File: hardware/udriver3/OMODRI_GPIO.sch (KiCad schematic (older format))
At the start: 5 parts, among them J14 Conn_01x40, U1 TMS320F28388D, U15 TPD2E001, U16 TPD3E001, U6 TPD3E001

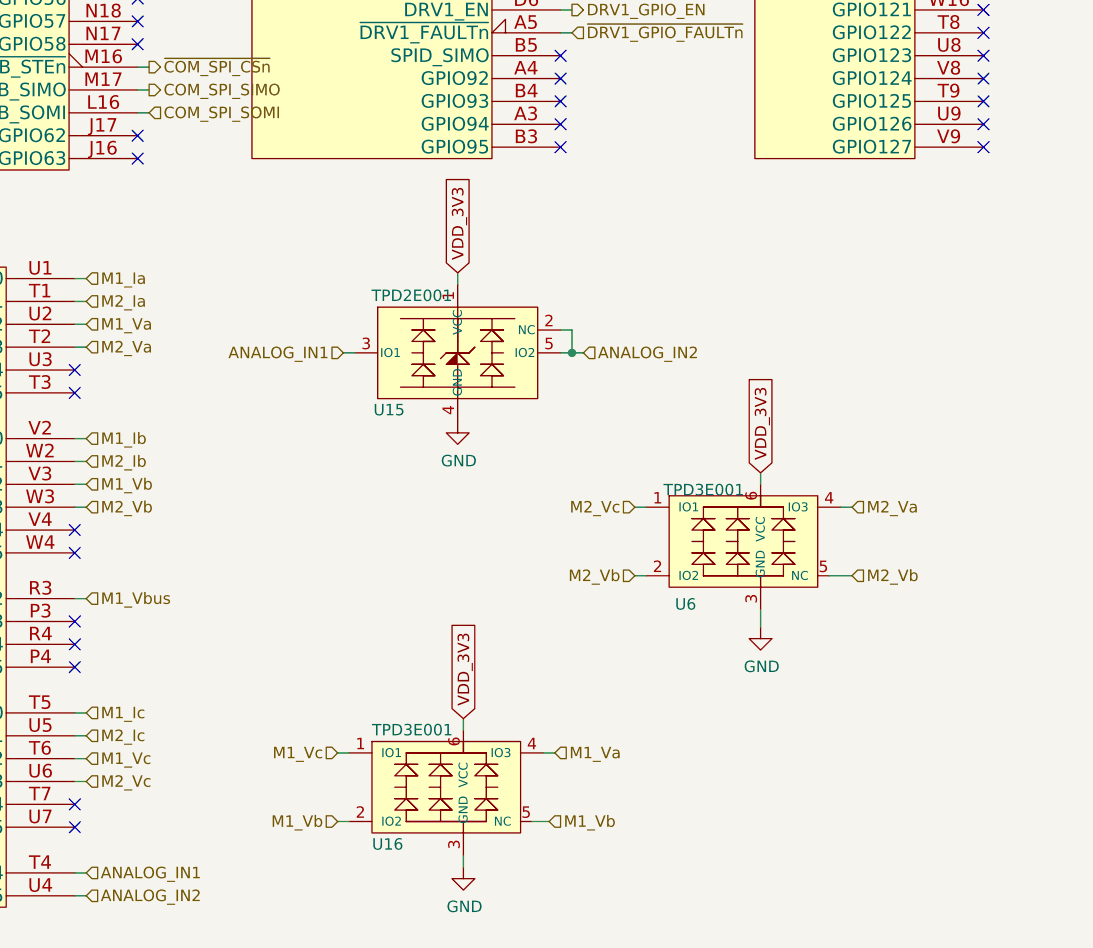
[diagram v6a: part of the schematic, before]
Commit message: Routing update. All analog and DRV signals are wired. TMS mcu decoupling capacitors are in place.
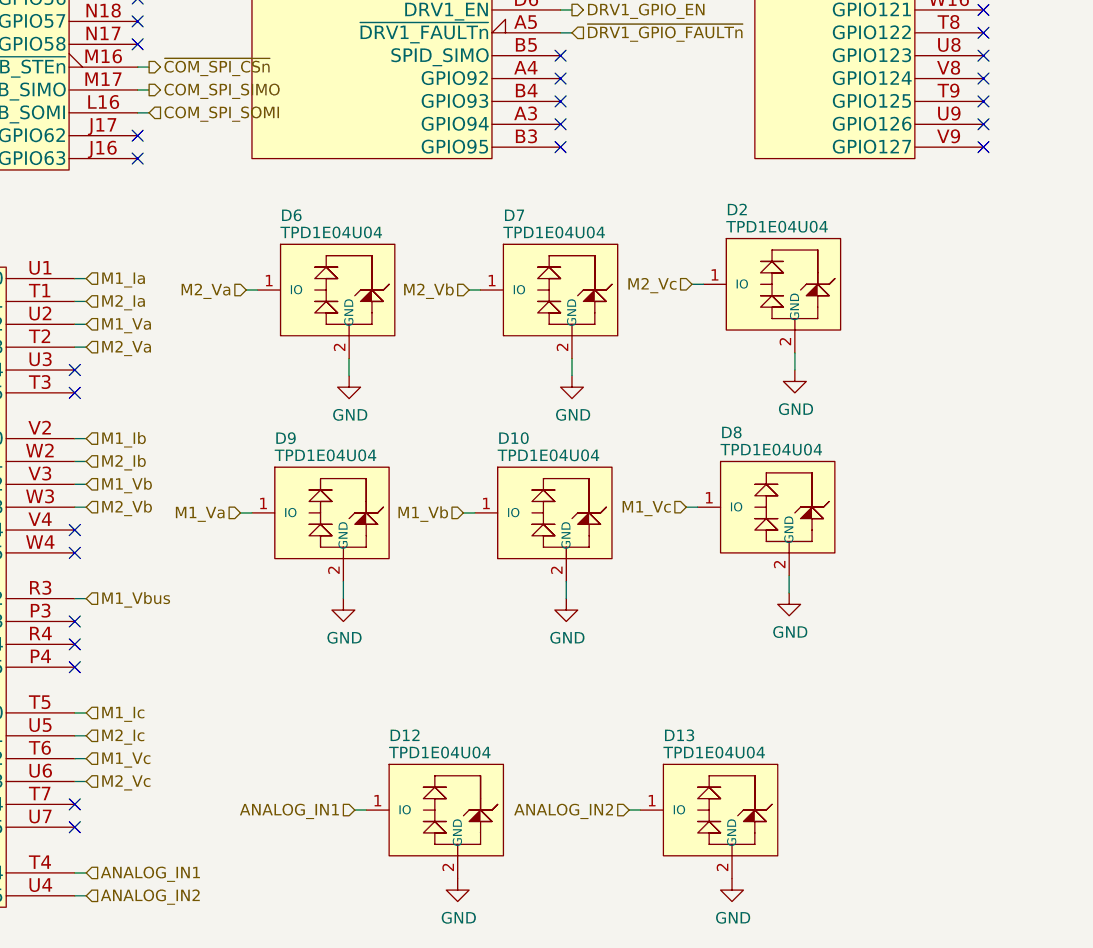
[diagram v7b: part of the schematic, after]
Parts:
- removed U15: TPD2E001, Package_SO:Texas_R-PDSO-N5, symbol omodri_lib:TPD2E001
- removed U16, U6: TPD3E001, udriver3:USON_6, symbol omodri_lib:TPD3E001
- added D10, D12, D13, D2, D6, D7, D8, D9: TPD1E04U04, Diode_SMD:D_0201_0603Metric, symbol omodri_lib:TPD1E04U04
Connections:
- net labels removed: VDD_3V3
- wire segments 177 -> 173

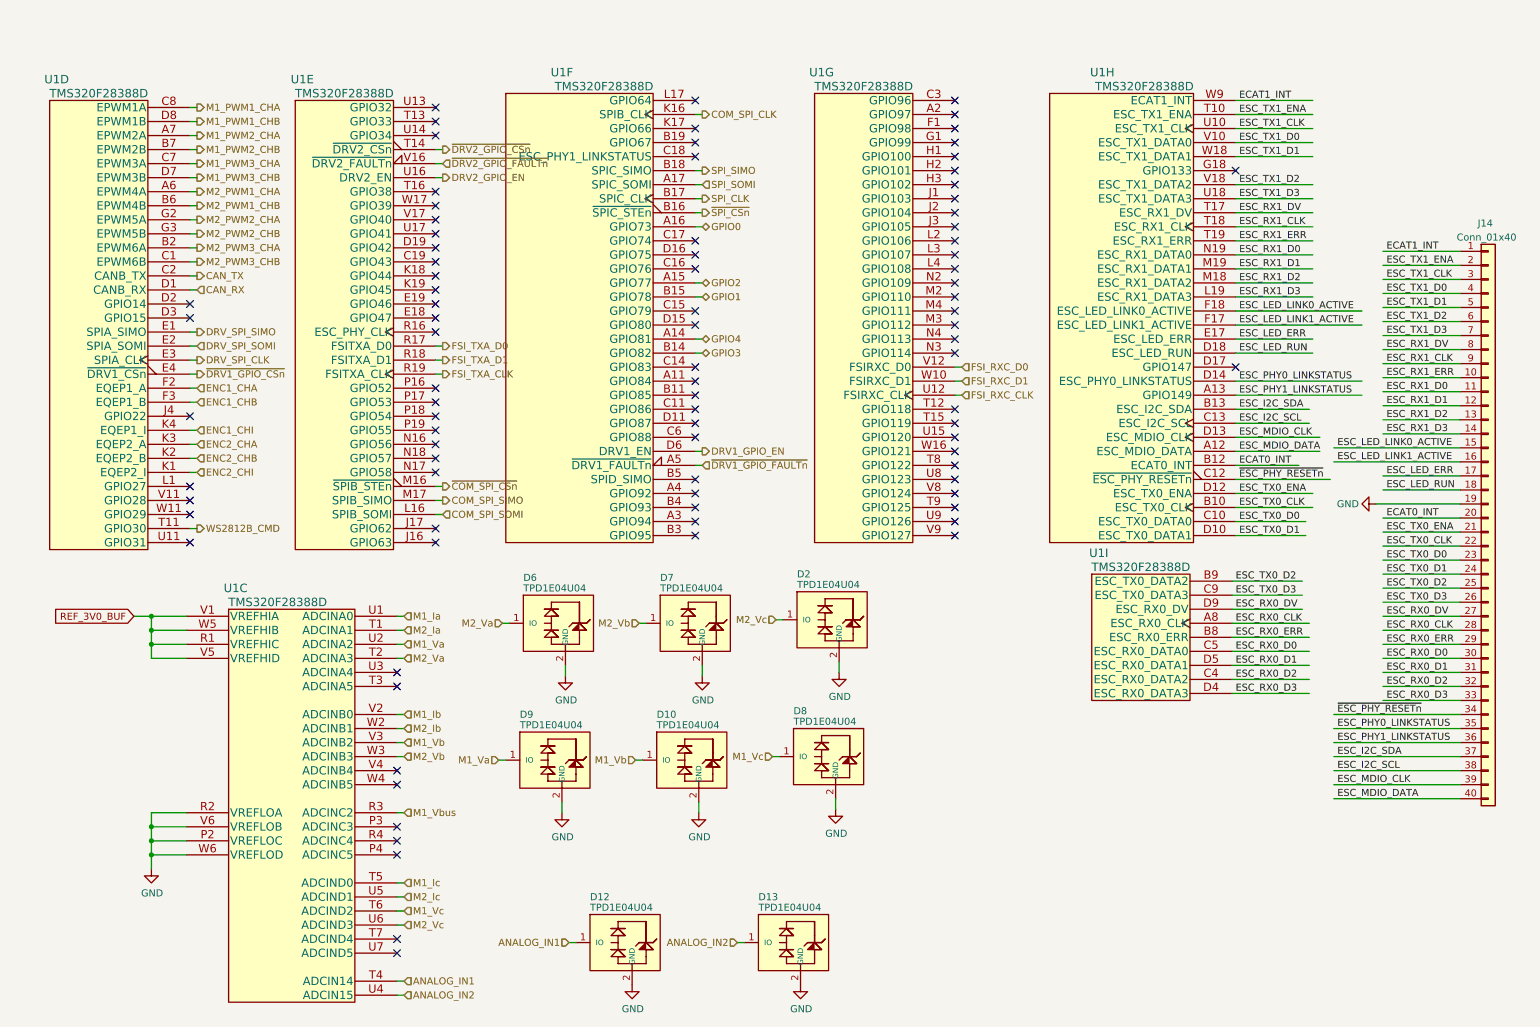
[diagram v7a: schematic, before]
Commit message: First release of the fully routed OMODRI PCB from LAAS. (8 layers)
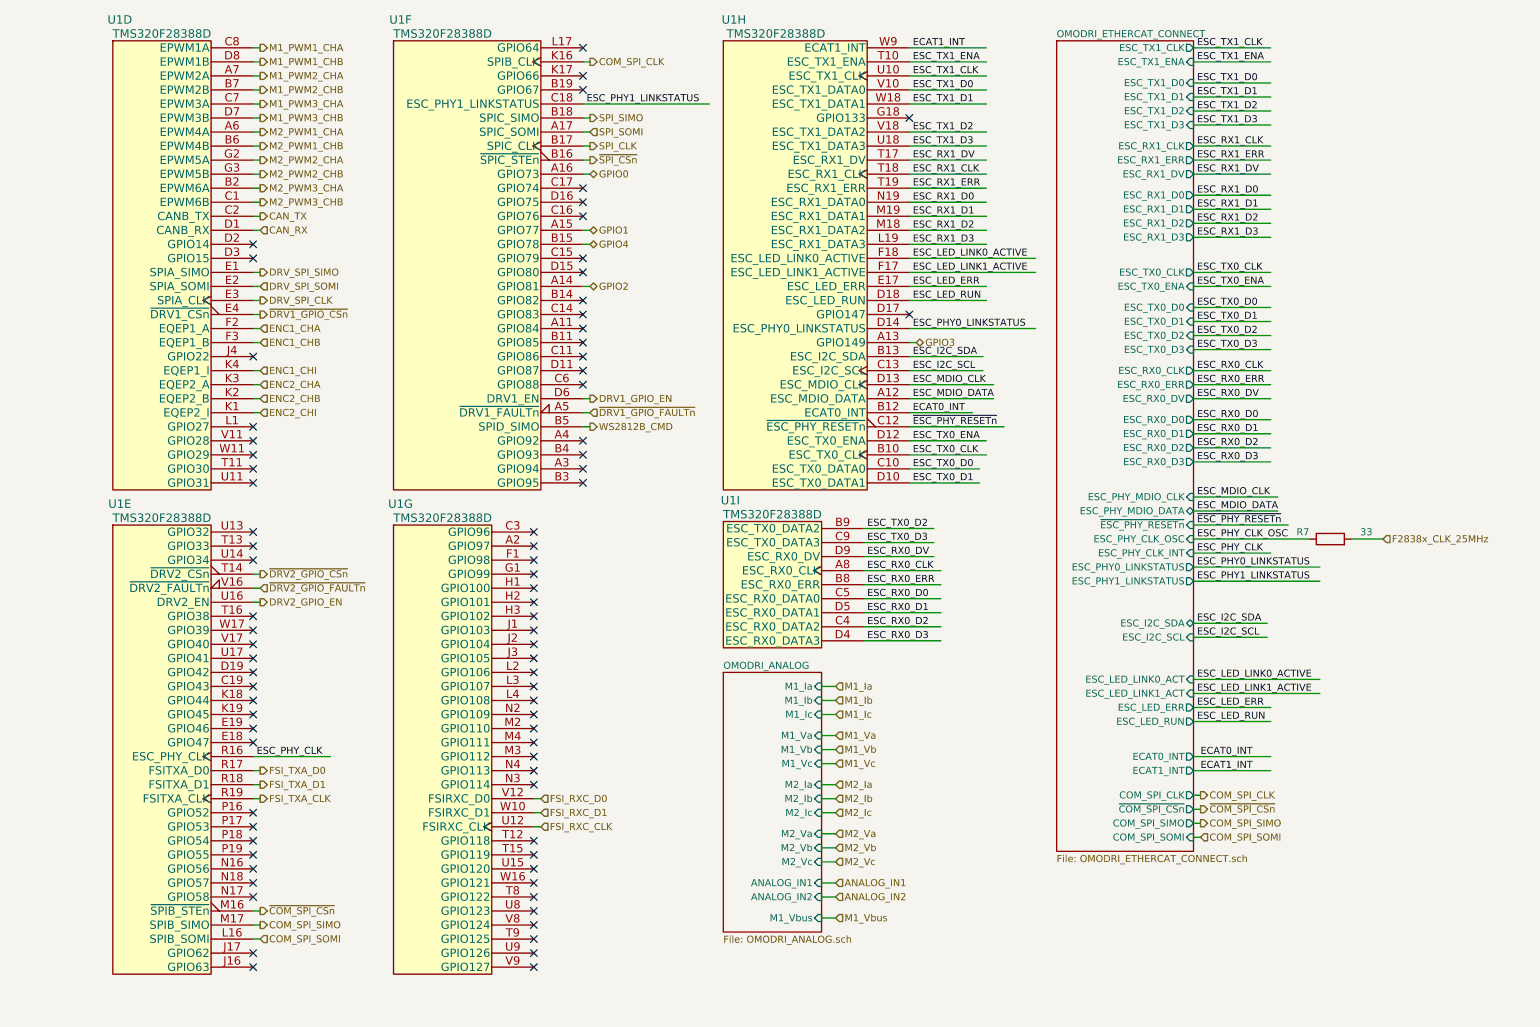
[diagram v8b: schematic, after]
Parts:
- removed D10, D12, D13, D2, D6, D7, D8, D9: TPD1E04U04, Diode_SMD:D_0201_0603Metric, symbol omodri_lib:TPD1E04U04
- removed J14: Conn_01x40, Connector_FFC-FPC:JAE_FF0841SA1_2Rows-41Pins_P0.40mm_Horizontal, symbol Connector_Generic:Conn_01x40
- removed unit 3 of U1
- added R7: 33, Resistor_SMD:R_0201_0603Metric, symbol Device:R
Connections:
- net labels added: ESC_PHY_CLK, ESC_PHY_CLK_OSC, F2838x_CLK_25MHz
- net labels removed: GND, REF_3V0_BUF
- wire segments 173 -> 150
- no-connect marks 90 -> 80
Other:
- moved on the sheet: U1D, U1E, U1F, U1G, U1H, U1I
